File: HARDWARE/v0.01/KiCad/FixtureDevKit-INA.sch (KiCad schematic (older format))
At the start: 60 parts, among them J27 INA_40, J28 INA_40, J29 INA_40, J30 INA_40, Q10 NTF2955-D, Q11 NTF2955-D, Q12 NTF2955-D, Q5 NTF2955-D, Q6 NTF2955-D, Q7 NTF2955-D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

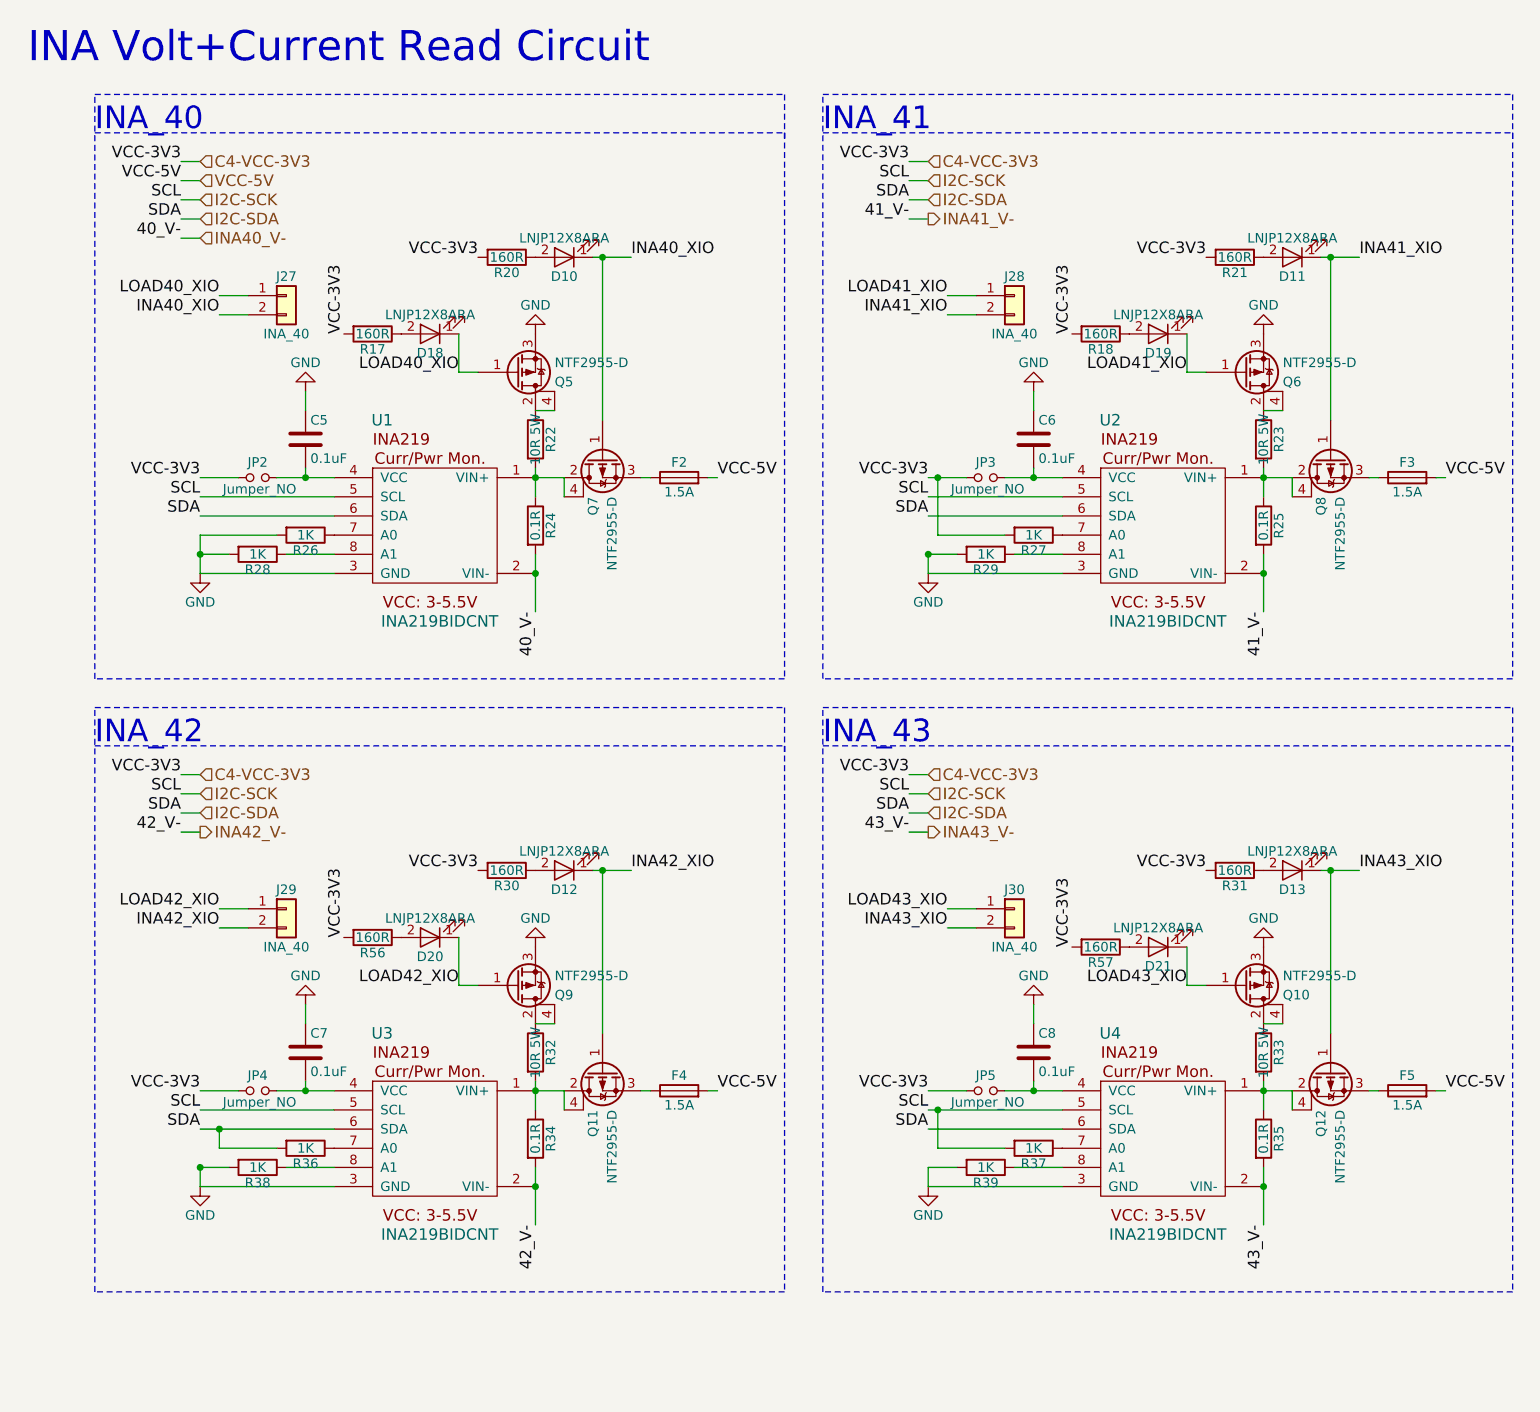
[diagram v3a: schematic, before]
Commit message: updating layout footprints and board outline
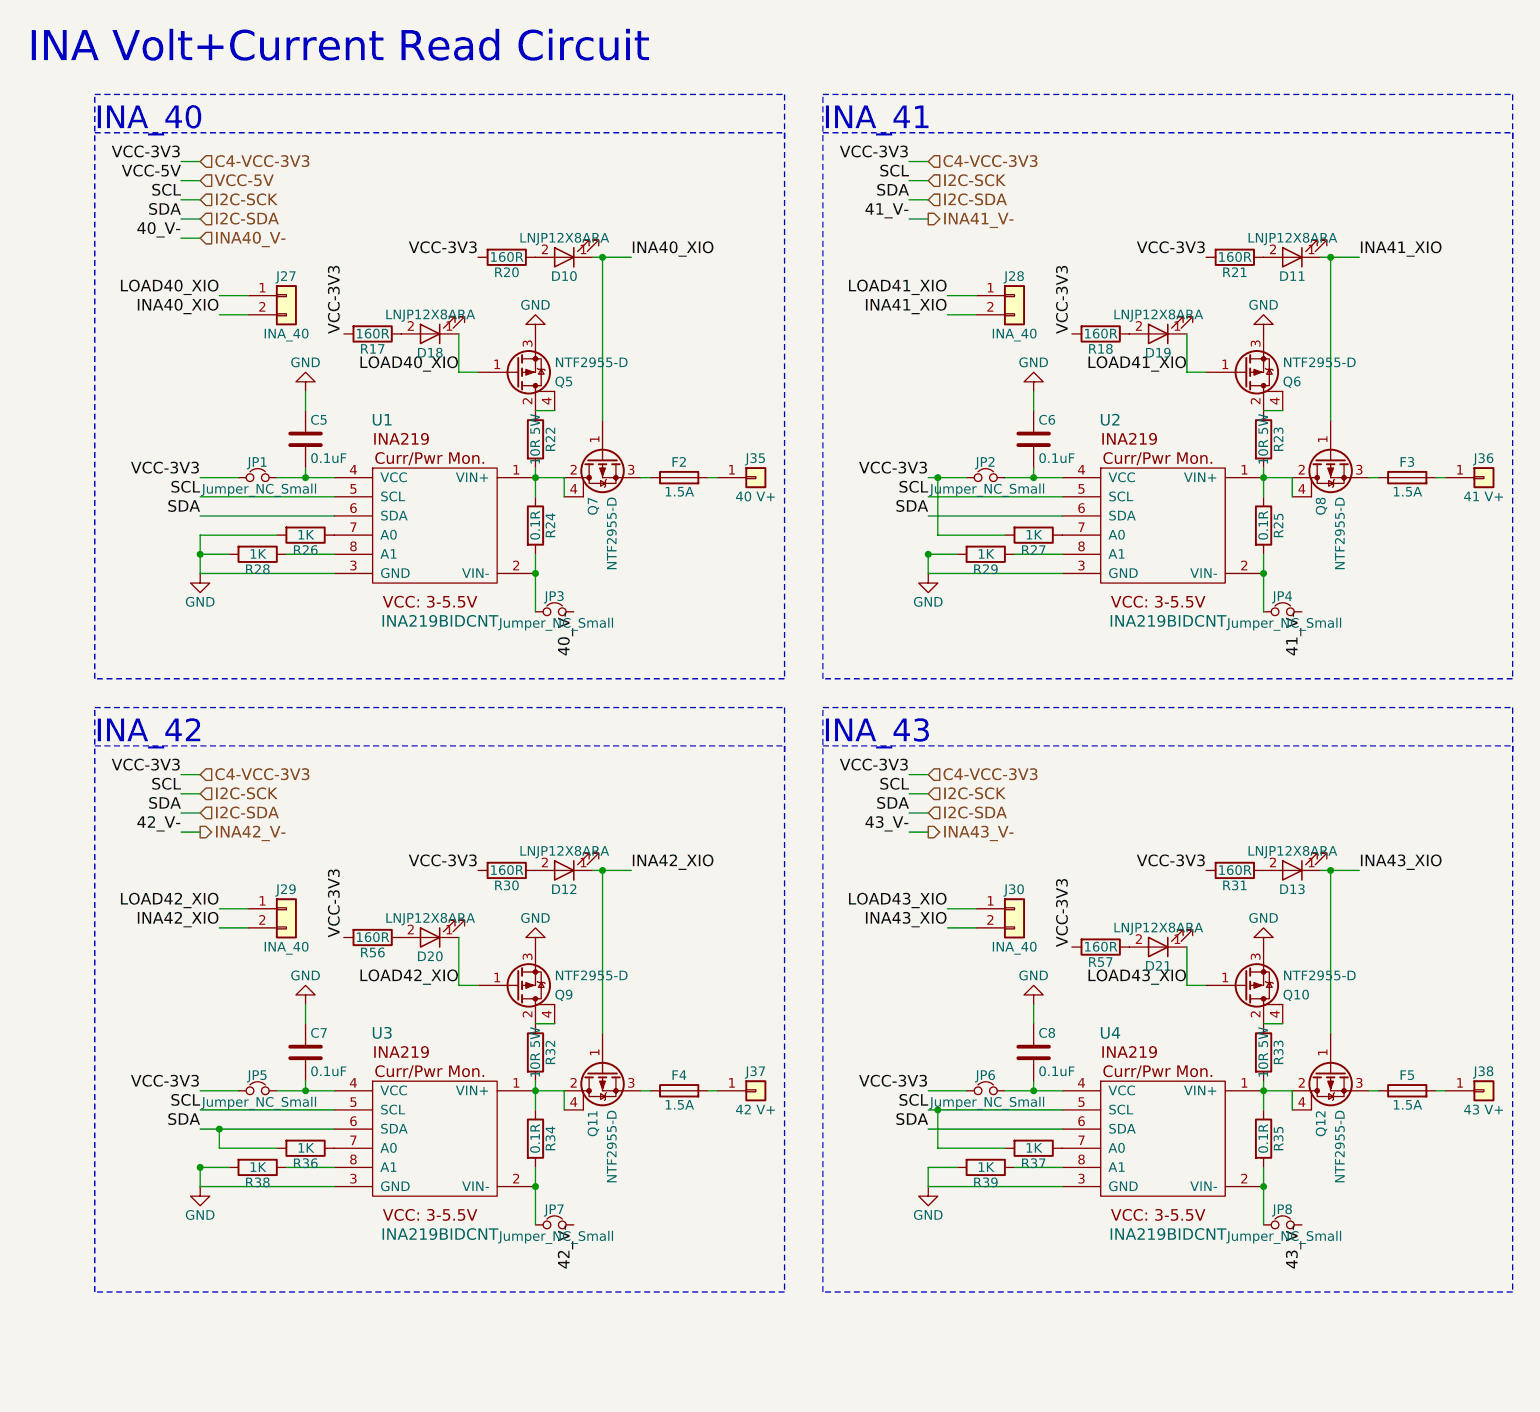
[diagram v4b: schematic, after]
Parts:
- removed JP2, JP3, JP4, JP5: Jumper_NO, Pin_Headers:Pin_Header_Straight_1x02_Pitch2.54mm, symbol Jumper_NO_Small
- added J35: 40 V+, Pin_Headers:Pin_Header_Straight_1x01_Pitch2.54mm, symbol Conn_01x01
- added J36: 41 V+, Pin_Headers:Pin_Header_Straight_1x01_Pitch2.54mm, symbol Conn_01x01
- added J37: 42 V+, Pin_Headers:Pin_Header_Straight_1x01_Pitch2.54mm, symbol Conn_01x01
- added J38: 43 V+, Pin_Headers:Pin_Header_Straight_1x01_Pitch2.54mm, symbol Conn_01x01
- added JP1, JP2, JP3, JP4, JP5, JP6, JP7, JP8: Jumper_NC_Small, ConnectedCutJumper:connectedCutJumper, symbol Jumper_NC_Small
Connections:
- net C4-VCC-3V3: now also JP1.1, JP2.1, JP5.1, JP6.1
- net INA40_V-: now also JP3.2; no longer R24.2, U1.2 (VIN-)
- net INA41_V-: now also JP4.2; no longer R25.2, U2.2 (VIN-)
- net INA42_V-: now also JP7.2; no longer R34.2, U3.2 (VIN-)
- net INA43_V-: now also JP8.2; no longer R35.2, U4.2 (VIN-)
- net VCC-5V: no longer F2.2, F3.2, F4.2, F5.2
- net at C5.2, U1.4 (VCC): now also JP1.2
- net at C6.2, U2.4 (VCC): now also JP2.2
- net at C7.2, U3.4 (VCC): now also JP5.2
- net at C8.2, U4.4 (VCC): now also JP6.2
- new net: JP3.1, R24.2, U1.2 (VIN-)
- new net: F2.2, J35.1 (Pin_1)
- new net: F4.2, J37.1 (Pin_1)
- new net: F5.2, J38.1 (Pin_1)
- new net: F3.2, J36.1 (Pin_1)
- new net: JP4.1, R25.2, U2.2 (VIN-)
- new net: JP7.1, R34.2, U3.2 (VIN-)
- new net: JP8.1, R35.2, U4.2 (VIN-)
